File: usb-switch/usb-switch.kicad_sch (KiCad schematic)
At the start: 5 parts, among them U1 LTC4317, U2 LTC4317, U3 PCA9537, U4 RP2040, X1 ASDMB-24MHz

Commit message: Starting to look closer to completion
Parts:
- added U5, U7: LTC4317, Package_DFN_QFN:DFN-16-1EP_3x5mm_P0.5mm_EP1.66x4.4mm, symbol Interface_Expansion:LTC4317
- added U6: PCA9537, Package_SO:TSSOP-10_3x3mm_P0.5mm, symbol Interface_Expansion:PCA9537
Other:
- added sheet downstream_port1 (downstream_port.kicad_sch)
- added sheet downstream_port2 (downstream_port.kicad_sch)
- added sheet downstream_port3 (downstream_port.kicad_sch)
- sheet downstream_port ports: added CONTROL{I2C INT}, UP_USB1{USB SS OVR}, UP_USB2{USB SS OVR}, UP_USB3{USB SS OVR}, UP_USB4{USB SS OVR}; removed none
- title: (none) -> Cursed USB Switch Main Board
- moved on the sheet: U1, U2, U3

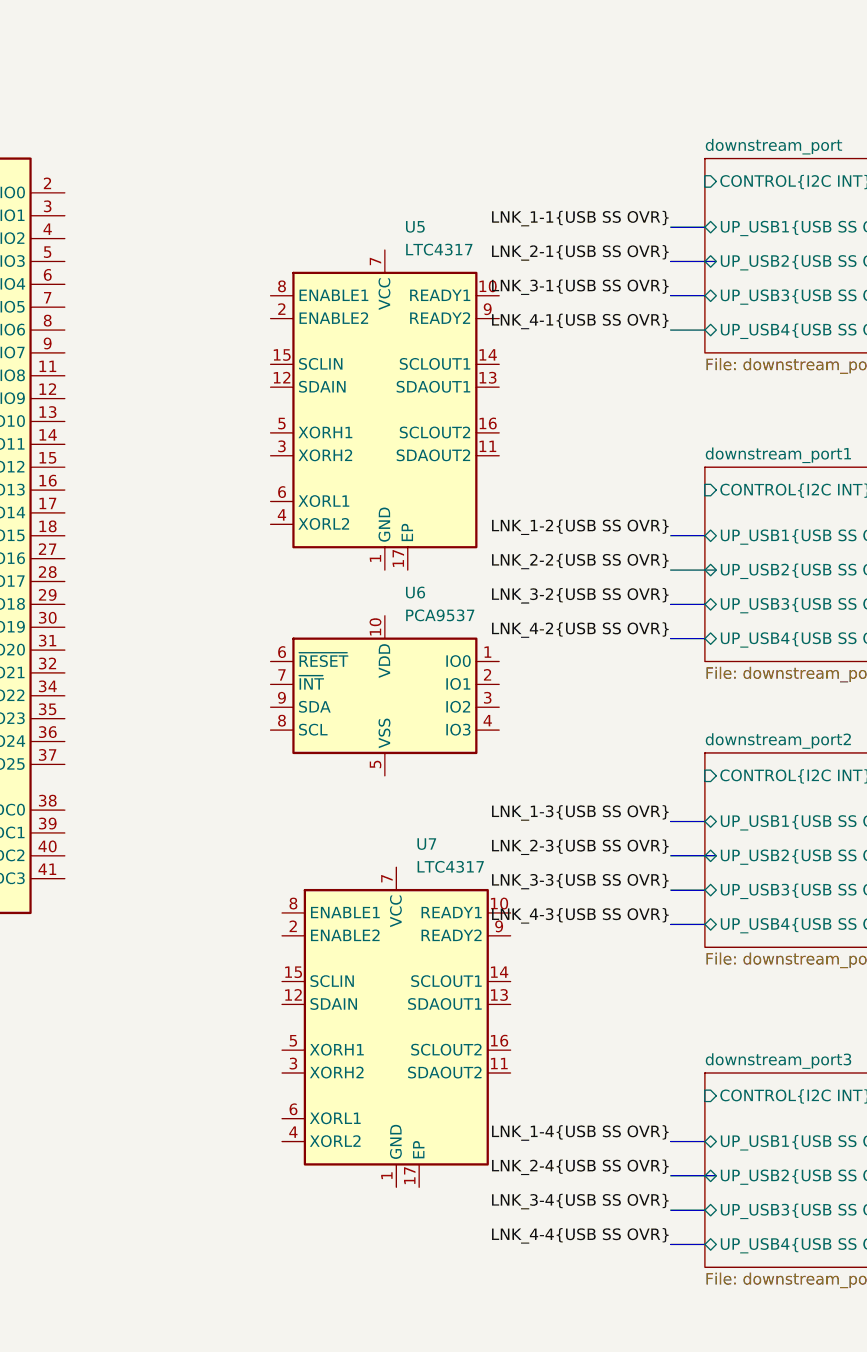
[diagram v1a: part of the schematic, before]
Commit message: Added some missing I2C and interrupt connections, further organizing of PCB layout
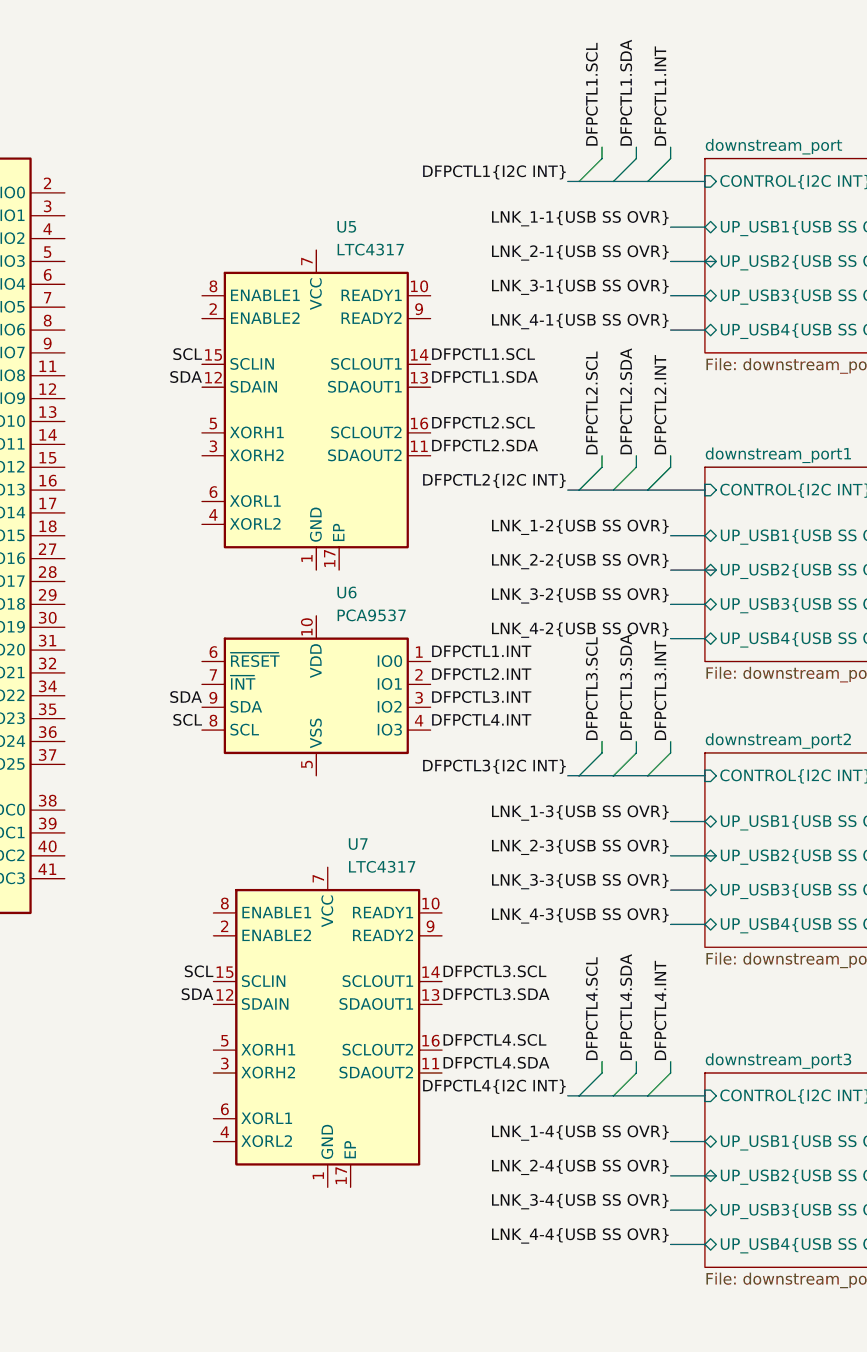
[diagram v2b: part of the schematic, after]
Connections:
- net SCL: now also U5.15 (SCLIN), U6.8 (SCL), U7.15 (SCLIN)
- net SDA: now also U5.12 (SDAIN), U6.9 (SDA), U7.12 (SDAIN)
- net DFPCTL2.SDA: now reaches U5.11 (SDAOUT2)
- net DFPCTL1.SDA: now reaches U5.13 (SDAOUT1)
- net DFPCTL1.SCL: now reaches U5.14 (SCLOUT1)
- net DFPCTL2.SCL: now reaches U5.16 (SCLOUT2)
- net DFPCTL4.SDA: now reaches U7.11 (SDAOUT2)
- net DFPCTL3.SDA: now reaches U7.13 (SDAOUT1)
- net DFPCTL3.SCL: now reaches U7.14 (SCLOUT1)
- net DFPCTL4.SCL: now reaches U7.16 (SCLOUT2)
- net DFPCTL1.INT: now reaches U6.1 (IO0)
- net DFPCTL2.INT: now reaches U6.2 (IO1)
- net DFPCTL3.INT: now reaches U6.3 (IO2)
- net DFPCTL4.INT: now reaches U6.4 (IO3)
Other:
- moved on the sheet: U5, U6, U7
